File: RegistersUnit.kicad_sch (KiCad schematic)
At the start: 20 parts, among them U23 74LS139, U24 74LS139, U25 74LS08, U26 74LS00, U57 74LS377, U58 74LS541, U59 74LS377, U60 74LS541, U61 74LS377, U62 74LS377, U63 74LS541, U64 74LS541

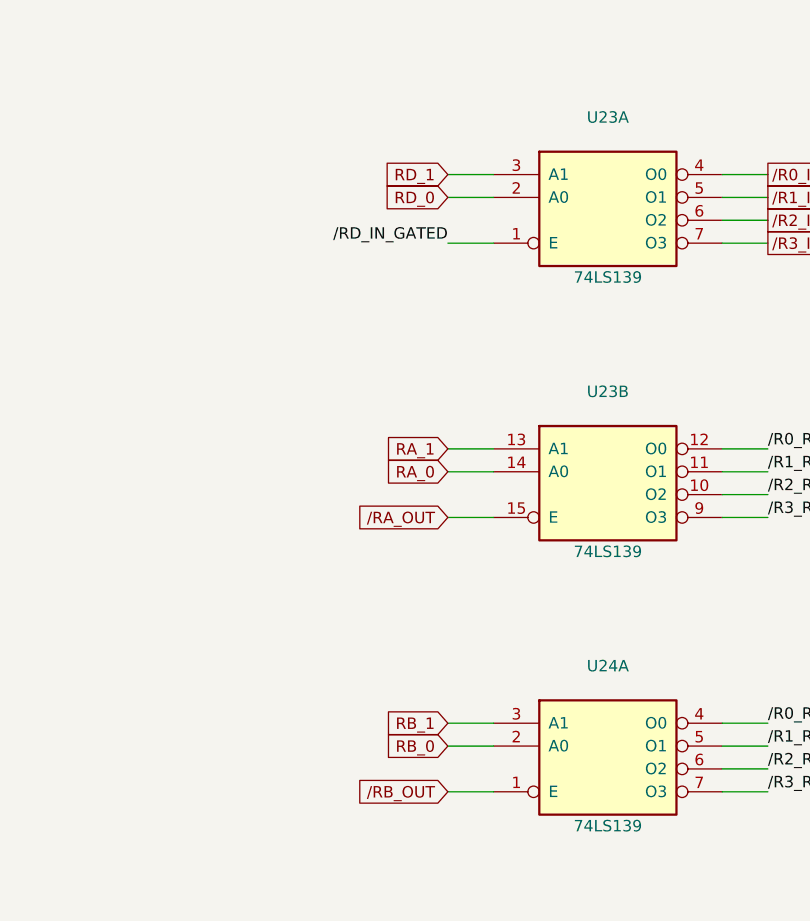
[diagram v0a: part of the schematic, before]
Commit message: Cleans up and restructures schematics
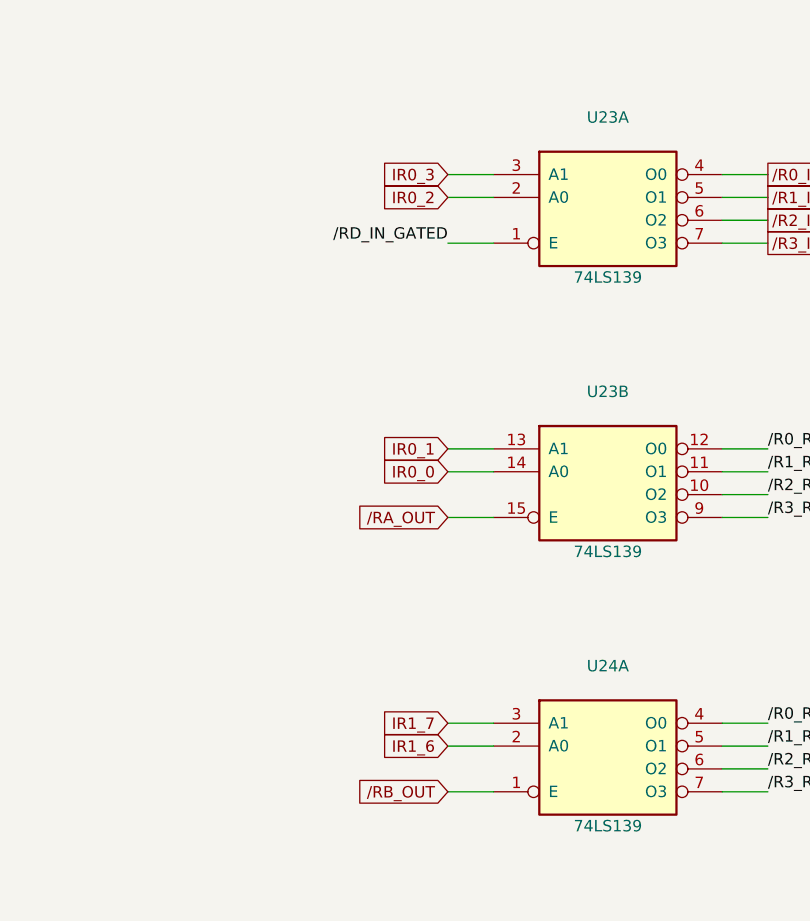
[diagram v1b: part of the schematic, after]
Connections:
- net RA_0 renamed IR0_0
- net RA_1 renamed IR0_1
- net RB_0 renamed IR1_6
- net RB_1 renamed IR1_7
- net RD_0 renamed IR0_2
- net RD_1 renamed IR0_3

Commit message: Fixes Gate symbol refs and adds backplane definition
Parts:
- removed U23, U24: 74LS139, Package_DIP:DIP-16_W7.62mm, symbol 74xx:74LS139
- removed U25: 74LS08, Package_DIP:DIP-14_W7.62mm, symbol 74xx:74LS08
- removed U26: 74LS00, Package_DIP:DIP-14_W7.62mm, symbol 74xx:74LS00
- added U1, U2: 74LS139, symbol 74xx:74LS139
- added U3, U4: 74LS08, symbol 74xx:74LS08
- renumbered C49 to C?, C45 to C?, C52 to C?, C51 to C?, C47 to C?, C50 to C?, C48 to C?, C46 to C?, U57 to U?, U58 to U?, U59 to U?, U60 to U?, U61 to U?, U62 to U?, U63 to U?, U64 to U?
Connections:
- net GND: now also U1.8 (GND), U2.13 (A1), U2.14 (A0), U2.8 (GND), U3.7 (GND), U4.7 (GND)
- net IR0_0: now also U1.14 (A0)
- net IR0_1: now also U1.13 (A1)
- net IR0_2: now also U1.2 (A0)
- net IR0_3: now also U1.3 (A1)
- net IR1_6: now also U2.2 (A0)
- net IR1_7: now also U2.3 (A1)
- net RD_IN: now also U4.3
- net VCC: now also U1.16 (VCC), U2.15 (E), U2.16 (VCC), U3.14 (VCC), U4.14 (VCC)
- net /R0_IN: now also U1.4 (O0)
- net /R0_OUT: now also U3.3
- net /R0_RA: now also U1.12 (O0)
- net /R0_RB: now also U2.4 (O0)
- net /R1_IN: now also U1.5 (O1)
- net /R1_OUT: now also U3.6
- net /R1_RA: now also U1.11 (O1)
- net /R1_RB: now also U2.5 (O1)
- net /R2_IN: now also U1.6 (O2)
- net /R2_OUT: now also U3.8
- net /R2_RA: now also U1.10 (O2)
- net /R2_RB: now also U2.6 (O2)
- net /R3_IN: now also U1.7 (O3)
- net /R3_OUT: now also U3.11
- net /R3_RA: now also U1.9 (O3)
- net /R3_RB: now also U2.7 (O3)
- net /RA_OUT: now also U1.15 (E)
- net /RB_OUT: now also U2.1 (E)
- net /RD_IN_GATED: now also U1.1 (E), U4.6
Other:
- note added: "GENERAL PURPOSE REGSITERS"
- note added: "REGISTER SELECTS"
- moved on the sheet: C?, U?
